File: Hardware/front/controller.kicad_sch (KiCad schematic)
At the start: 15 parts

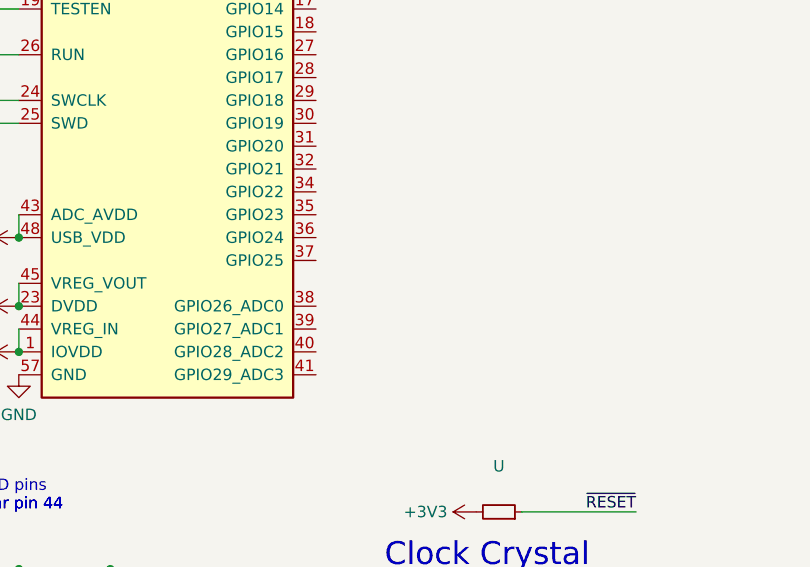
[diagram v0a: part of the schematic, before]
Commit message: hw: more front panel stuff
- fixed the mirrored pinout for the connector to the controller board

- Replaced a few capacitors to reduce BOM count

- Start connecting signals to RP2040, including the flash connection
  (dedicated to it)
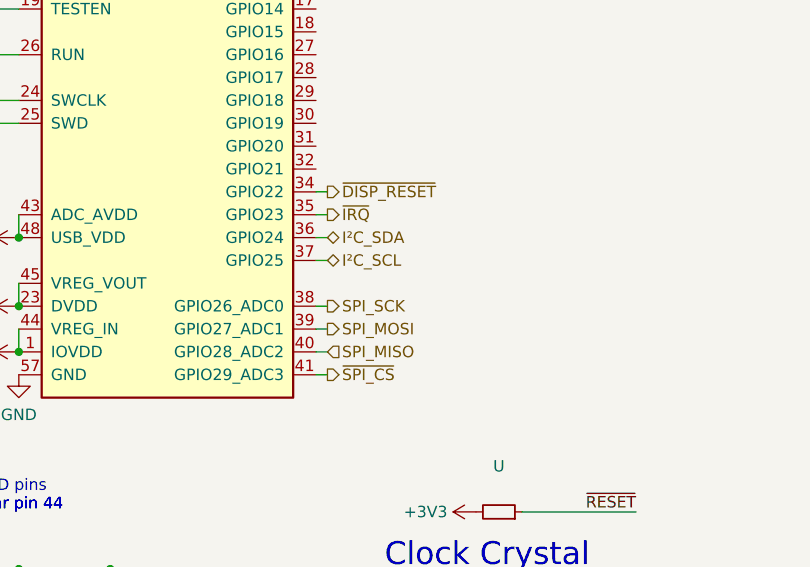
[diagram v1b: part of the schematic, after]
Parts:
- U: JLCPCB (none) -> C19666
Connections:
- net ~{DISP_RESET}: now reaches U.34 (GPIO22)
- net ~{IRQ}: now reaches U.35 (GPIO23)
- net I²C_SDA: now reaches U.36 (GPIO24)
- net I²C_SCL: now reaches U.37 (GPIO25)
- net SPI_SCK: now reaches U.38 (GPIO26_ADC0)
- net SPI_MOSI: now reaches U.39 (GPIO27_ADC1)
- net SPI_MISO: now reaches U.40 (GPIO28_ADC2)
- net ~{SPI_CS}: now reaches U.41 (GPIO29_ADC3)
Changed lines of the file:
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@@
+    (stroke (width 0) (type default))
+  )
+  (wire (pts (xy 68.58 93.98) (xy 69.85 93.98))
     (stroke (width 0) (type default))
   )
@@
     (stroke (width 0) (type default))
   )
+  (wire (pts (xy 68.58 91.44) (xy 69.85 91.44))
+    (stroke (width 0) (type default))
+  )
   (wire (pts (xy 35.56 147.32) (xy 45.72 147.32))
     (stroke (width 0) (type default))
@@
     (stroke (width 0) (type default))
   )
+  (wire (pts (xy 68.58 78.74) (xy 69.85 78.74))
+    (stroke (width 0) (type default))
+  )
   (wire (pts (xy 101.6 173.355) (xy 114.3 173.355))
     (stroke (width 0) (type default))
@@
     (stroke (width 0) (type default))
   )
+  (wire (pts (xy 68.58 99.06) (xy 69.85 99.06))
+    (stroke (width 0) (type default))
+  )
   (wire (pts (xy 45.72 125.73) (xy 55.88 125.73))
     (stroke (width 0) (type default))
@@
     (stroke (width 0) (type default))
   )
+  (wire (pts (xy 68.58 81.28) (xy 69.85 81.28))
+    (stroke (width 0) (type default))
+  )
   (wire (pts (xy 42.545 174.625) (xy 55.245 174.625))
     (stroke (width 0) (type default))
   )
+  (wire (pts (xy 68.58 96.52) (xy 69.85 96.52))
+    (stroke (width 0) (type default))
+  )
   (wire (pts (xy 35.56 36.83) (xy 22.86 36.83))
     (stroke (width 0) (type default))
@@
     (stroke (width 0) (type default))
   )
+  (wire (pts (xy 68.58 83.82) (xy 69.85 83.82))
+    (stroke (width 0) (type default))
+  )
   (wire (pts (xy 35.56 34.29) (xy 22.86 34.29))
     (stroke (width 0) (type default))
@@
   )
   (wire (pts (xy 25.4 147.32) (xy 35.56 147.32))
+    (stroke (width 0) (type default))
+  )
+  (wire (pts (xy 68.58 86.36) (xy 69.85 86.36))
     (stroke (width 0) (type default))
   )
@@
   (label "XIN" (at 80.01 133.35 0) (fields_autoplaced)
     (effects (font (size 1.27 1.27)) (justify left bottom))
+  )
+  (hierarchical_label "I²C_SCL" (shape bidirectional) (at 69.85 86.36 0) (fields_autoplaced)
+    (effects (font (size 1.27 1.27)) (justify left))
+  )
+  (hierarchical_label "SPI_MOSI" (shape output) (at 69.85 93.98 0) (fields_autoplaced)
+    (effects (font (size 1.27 1.27)) (justify left))
+  )
+  (hierarchical_label "I²C_SDA" (shape bidirectional) (at 69.85 83.82 0) (fields_autoplaced)
+    (effects (font (size 1.27 1.27)) (justify left))
+  )
+  (hierarchical_label "SPI_SCK" (shape output) (at 69.85 91.44 0) (fields_autoplaced)
+    (effects (font (size 1.27 1.27)) (justify left))
+  )
+  (hierarchical_label "~{SPI_CS}" (shape output) (at 69.85 99.06 0) (fields_autoplaced)
+    (effects (font (size 1.27 1.27)) (justify left))
+  )
+  (hierarchical_label "~{IRQ}" (shape output) (at 69.85 81.28 0) (fields_autoplaced)
+    (effects (font (size 1.27 1.27)) (justify left))
+  )
+  (hierarchical_label "~{DISP_RESET}" (shape output) (at 69.85 78.74 0) (fields_autoplaced)
+    (effects (font (size 1.27 1.27)) (justify left))
+  )
+  (hierarchical_label "SPI_MISO" (shape input) (at 69.85 96.52 0) (fields_autoplaced)
+    (effects (font (size 1.27 1.27)) (justify left))
   )
   (symbol (lib_id "Device:C_Small") (at 55.88 123.19 0) (mirror y) (unit 1)
@@
       (effects (font (size 1.27 1.27)) hide)
     )
+    (property "JLCPCB" "C19666" (id 5) (at 25.4 123.19 0)
+      (effects (font (size 1.27 1.27)) hide)
+    )
     (pin "1")
     (pin "2")
@@
       (effects (font (size 1.27 1.27)) hide)
     )
+    (property "JLCPCB" "C19666" (id 5) (at 25.4 144.78 0)
+      (effects (font (size 1.27 1.27)) hide)
+    )

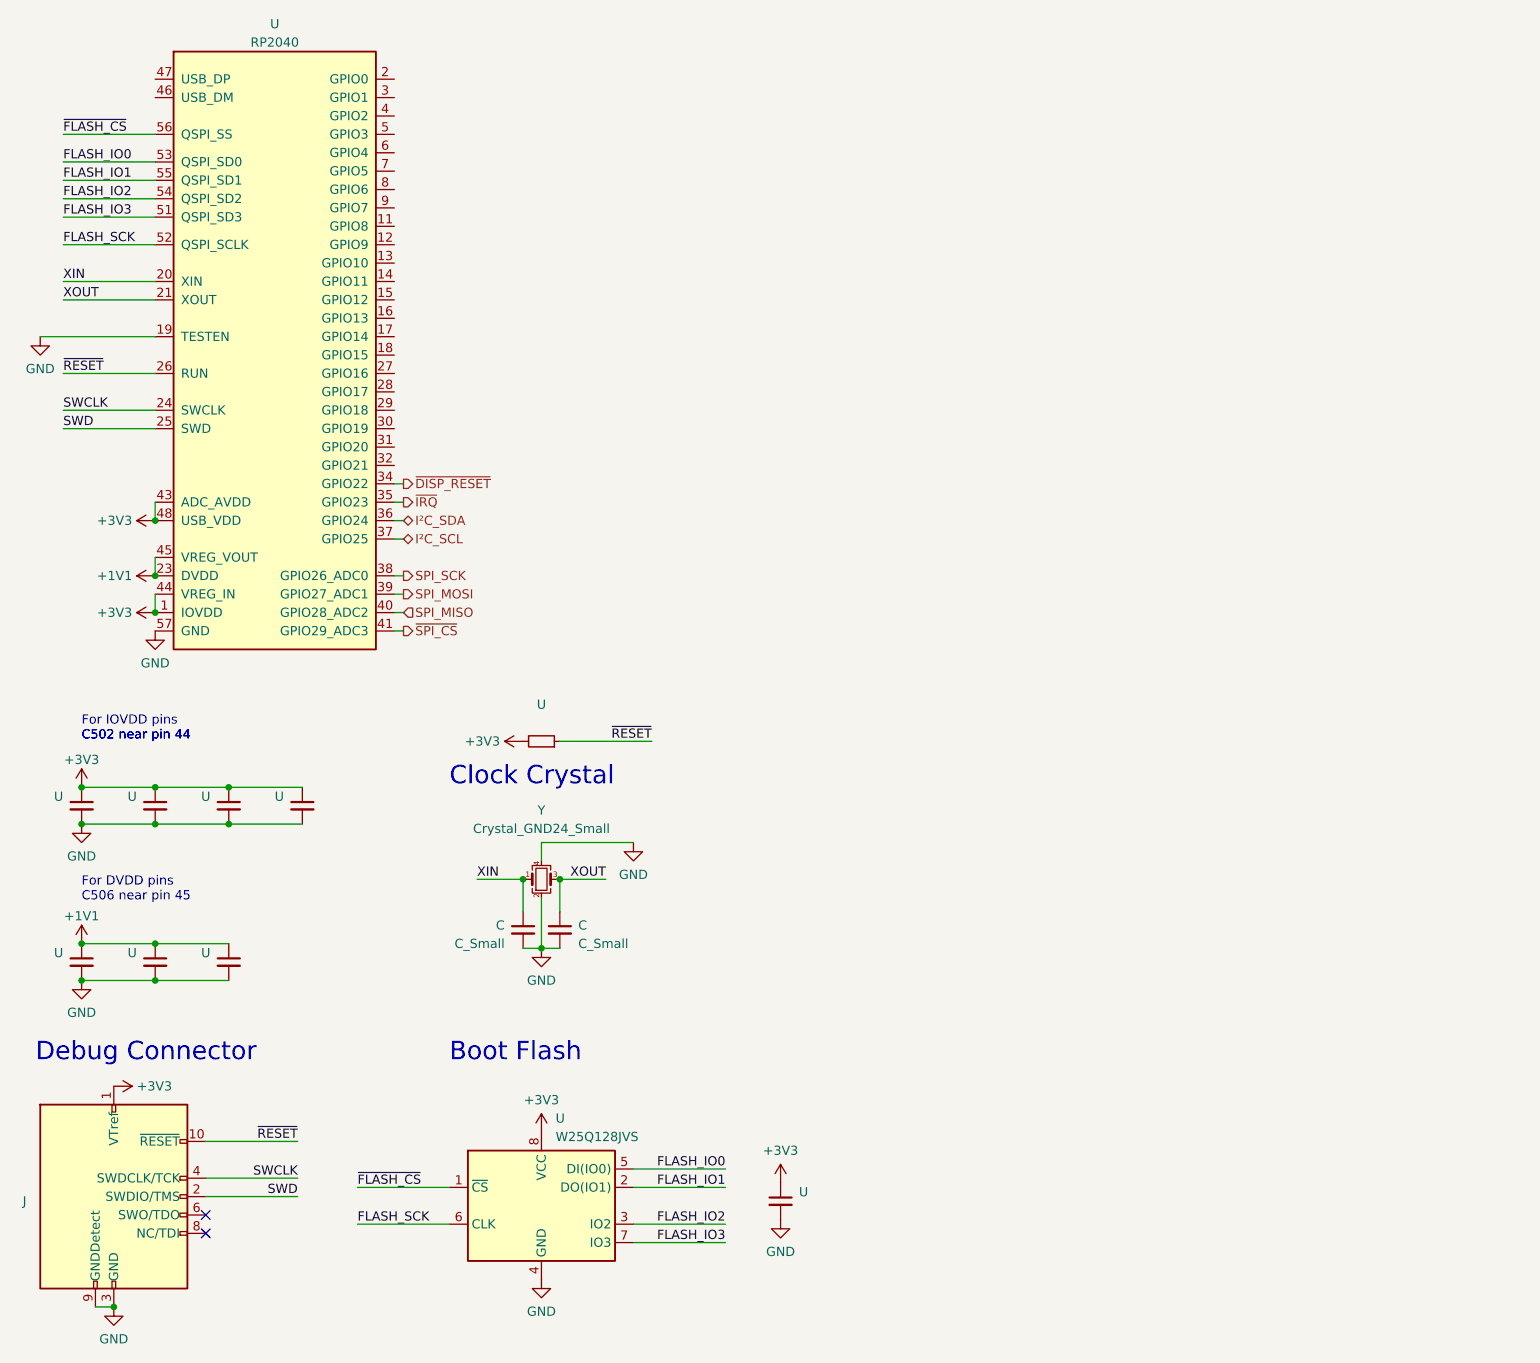
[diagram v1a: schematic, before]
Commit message: hw: First pass at new front panel
- Finished routing all signals on the front panel

- Put back the LED controller (PCA9955B) since that's a very nice and
  convenient way to drive the LEDs; it's driven via a "private" I2C bus
  from the RP2040 instead of the host controlling it.

  The touch panel controller is also hanging off this private bus so we
  can deal with it.

- Made trigger LED bicolor (green/orange)
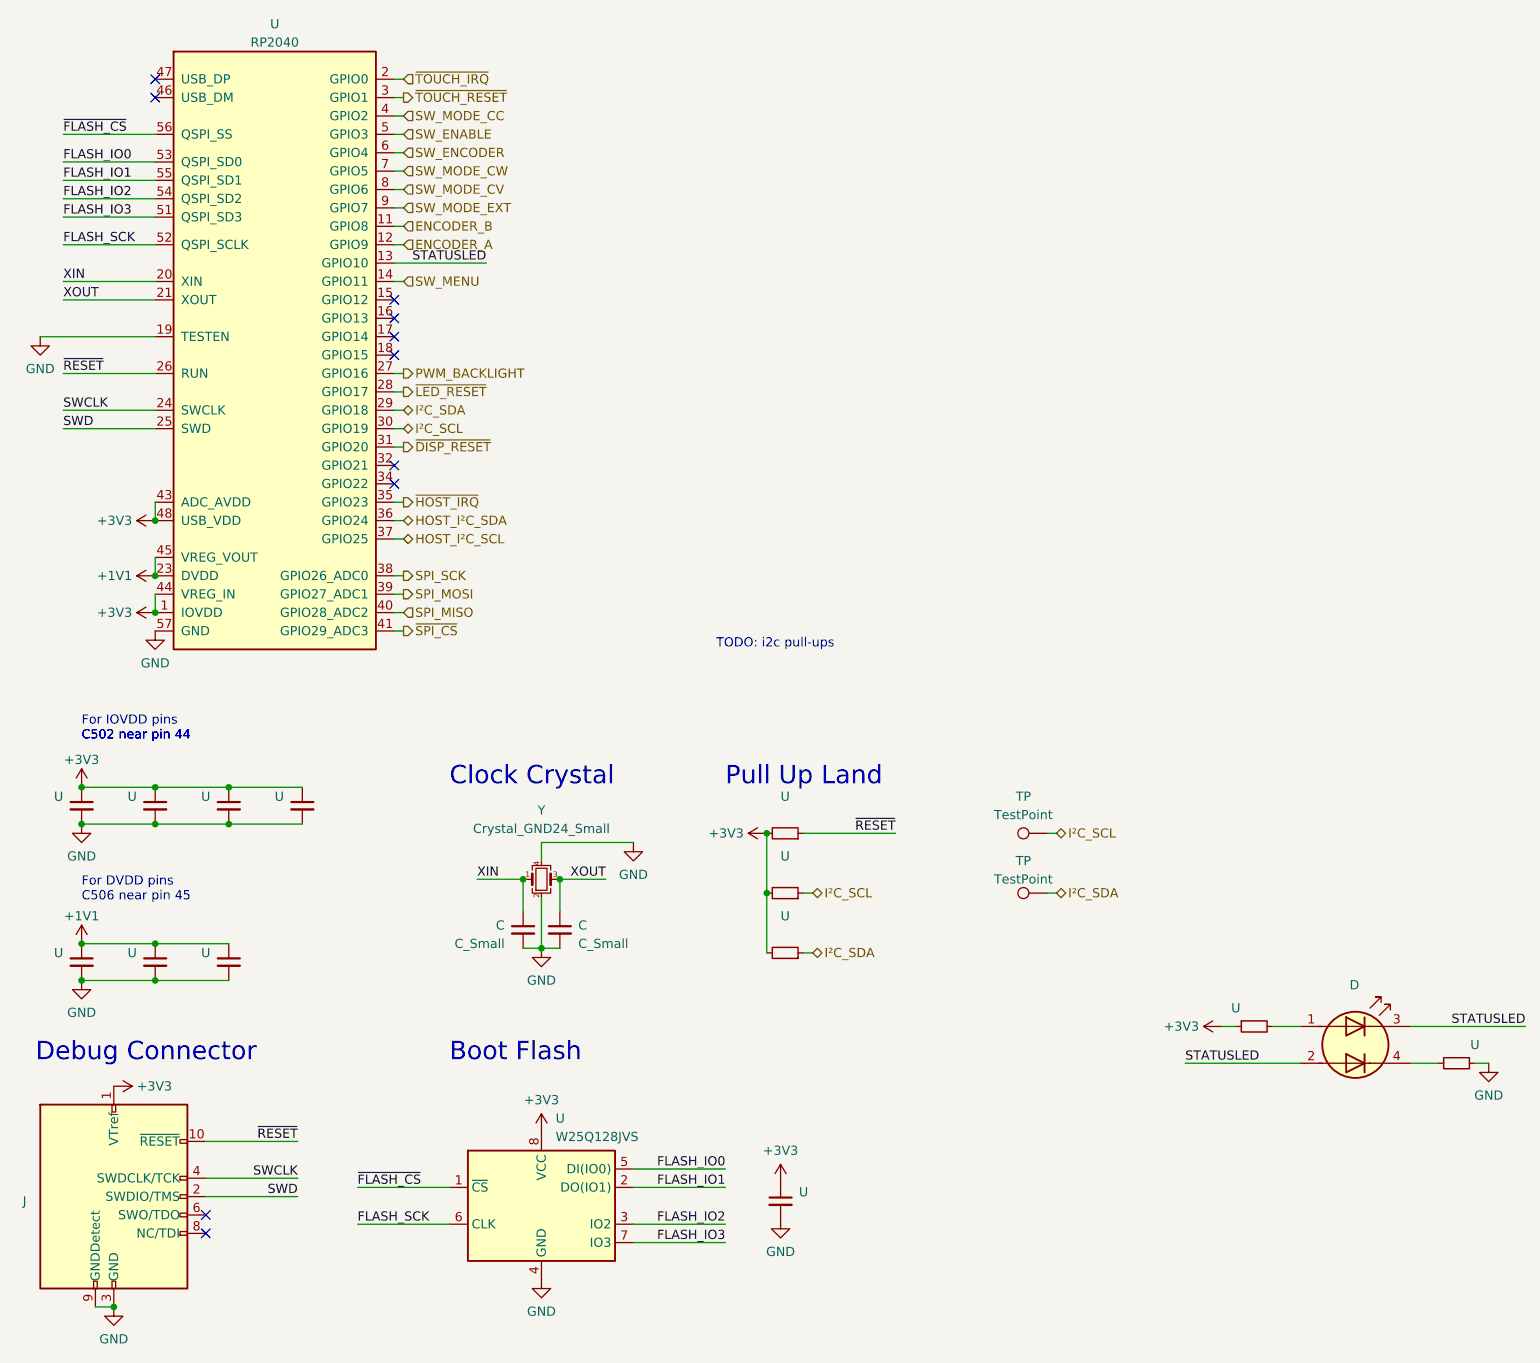
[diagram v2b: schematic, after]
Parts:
- added D: LED_Dual_AAKK, symbol Device:LED_Dual_AAKK
- added TP (x2): TestPoint, symbol Connector:TestPoint
- added U (x4): (no value), symbol Device:R_Small
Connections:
- net +3V3: now also U.1, U.2, U.2
- net GND: now also U.1
- net I²C_SCL: now also U.30 (GPIO19), TP.1, U.1; no longer U.37 (GPIO25)
- net I²C_SDA: now also U.29 (GPIO18), TP.1, U.1; no longer U.36 (GPIO24)
- net ~{DISP_RESET}: now also U.31 (GPIO20); no longer U.34 (GPIO22)
- net ENCODER_B: now reaches U.11 (GPIO8)
- net ENCODER_A: now reaches U.12 (GPIO9)
- net STATUSLED: now reaches U.13 (GPIO10)
- net STATUSLED: now also D.2 (A2), D.3 (K1)
- net SW_MENU: now reaches U.14 (GPIO11)
- net ~{TOUCH_IRQ}: now reaches U.2 (GPIO0)
- net PWM_BACKLIGHT: now reaches U.27 (GPIO16)
- net ~{LED_RESET}: now reaches U.28 (GPIO17)
- net ~{TOUCH_RESET}: now reaches U.3 (GPIO1)
- net SW_MODE_CC: now reaches U.4 (GPIO2)
- net SW_ENABLE: now reaches U.5 (GPIO3)
- net SW_ENCODER: now reaches U.6 (GPIO4)
- net SW_MODE_CW: now reaches U.7 (GPIO5)
- net SW_MODE_CV: now reaches U.8 (GPIO6)
- net SW_MODE_EXT: now reaches U.9 (GPIO7)
- net ~{IRQ} renamed ~{HOST_IRQ}
- new net: D.1 (A1), U.2
- new net: D.4 (K2), U.2
- new net HOST_I²C_SCL: U.37 (GPIO25)
- new net HOST_I²C_SDA: U.36 (GPIO24)
- no-connect marks 2 -> 10
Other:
- note added: "Pull Up Land"
- note added: "TODO: i2c pull-ups"
- moved on the sheet: U

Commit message: updated front panel pinout
- added system reset, direct load on/off switch output lines

- added separate touch screen reset/interrupt lines (the touch
  controller gets to be driven by linux side)

- update footprint for ER-TFT040-1 display

  this tweaks the sizes of the openings and the text labels a bit to be
  prettier
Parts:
- U: JLCPCB (none) -> C14663
- U: JLCPCB (none) -> C2040
- U: JLCPCB (none) -> C97521
- U: JLCPCB (none) -> C21190
- U: JLCPCB (none) -> C25804
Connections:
- net ~{TOUCH_IRQ}: no longer names the net of U.2 (GPIO0)
- net ~{TOUCH_RESET} renamed ~{SYS_RESET}
- no-connect marks 10 -> 11
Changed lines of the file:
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@@
   (no_connect (at 42.545 179.705))
   (no_connect (at 35.56 22.86))
+  (no_connect (at 68.58 22.86))
   (no_connect (at 68.58 55.88))
   (no_connect (at 42.545 182.245))
@@
     (stroke (width 0) (type default))
   )
-  (wire (pts (xy 68.58 22.86) (xy 69.85 22.86))
-    (stroke (width 0) (type default))
-  )
   (wire (pts (xy 68.58 45.72) (xy 69.85 45.72))
     (stroke (width 0) (type default))
@@
     (stroke (width 0) (type default))
   )
+  (wire (pts (xy 86.36 133.35) (xy 86.36 137.795))
+    (stroke (width 0) (type default))
+  )
+  (wire (pts (xy 22.86 71.12) (xy 35.56 71.12))
+    (stroke (width 0) (type default))
+  )
+  (wire (pts (xy 68.58 43.18) (xy 69.85 43.18))
+    (stroke (width 0) (type default))
+  )
+  (wire (pts (xy 22.86 45.72) (xy 35.56 45.72))
+    (stroke (width 0) (type default))
+  )
+  (wire (pts (xy 22.86 63.5) (xy 35.56 63.5))
+    (stroke (width 0) (type default))
+  )
+  (wire (pts (xy 68.58 99.06) (xy 69.85 99.06))
+    (stroke (width 0) (type default))
+  )
+  (wire (pts (xy 45.72 125.73) (xy 55.88 125.73))
+    (stroke (width 0) (type default))
+  )
+  (wire (pts (xy 35.56 88.9) (xy 35.56 91.44))
+    (stroke (width 0) (type default))
+  )
+  (wire (pts (xy 35.56 125.73) (xy 45.72 125.73))
+    (stroke (width 0) (type default))
+  )
+  (wire (pts (xy 42.545 169.545) (xy 55.245 169.545))
+    (stroke (width 0) (type default))
+  )
+  (wire (pts (xy 68.58 63.5) (xy 69.85 63.5))
+    (stroke (width 0) (type default))
+  )
+  (wire (pts (xy 35.56 39.37) (xy 22.86 39.37))
+    (stroke (width 0) (type default))
+  )
+  (wire (pts (xy 217.805 158.75) (xy 219.71 158.75))
+    (stroke (width 0) (type default))
+  )
   (wire (pts (xy 68.58 25.4) (xy 69.85 25.4))
-    (stroke (width 0) (type default))
-  )
-  (wire (pts (xy 86.36 133.35) (xy 86.36 137.795))
-    (stroke (width 0) (type default))
-  )
-  (wire (pts (xy 22.86 71.12) (xy 35.56 71.12))
-    (stroke (width 0) (type default))
-  )
-  (wire (pts (xy 68.58 43.18) (xy 69.85 43.18))
-    (stroke (width 0) (type default))
-  )
-  (wire (pts (xy 22.86 45.72) (xy 35.56 45.72))
-    (stroke (width 0) (type default))
-  )
-  (wire (pts (xy 22.86 63.5) (xy 35.56 63.5))
-    (stroke (width 0) (type default))
-  )
-  (wire (pts (xy 68.58 99.06) (xy 69.85 99.06))
-    (stroke (width 0) (type default))
-  )
-  (wire (pts (xy 45.72 125.73) (xy 55.88 125.73))
-    (stroke (width 0) (type default))
-  )
-  (wire (pts (xy 35.56 88.9) (xy 35.56 91.44))
-    (stroke (width 0) (type default))
-  )
-  (wire (pts (xy 35.56 125.73) (xy 45.72 125.73))
-    (stroke (width 0) (type default))
-  )
-  (wire (pts (xy 42.545 169.545) (xy 55.245 169.545))
-    (stroke (width 0) (type default))
-  )
-  (wire (pts (xy 68.58 63.5) (xy 69.85 63.5))
-    (stroke (width 0) (type default))
-  )
-  (wire (pts (xy 35.56 39.37) (xy 22.86 39.37))
-    (stroke (width 0) (type default))
-  )
-  (wire (pts (xy 217.805 158.75) (xy 219.71 158.75))
     (stroke (width 0) (type default))
   )
@@
     (effects (font (size 1.27 1.27)) (justify left))
   )
-  (hierarchical_label "~{TOUCH_IRQ}" (shape input) (at 69.85 22.86 0) (fields_autoplaced)
+  (hierarchical_label "~{SYS_RESET}" (shape output) (at 69.85 25.4 0) (fields_autoplaced)
     (effects (font (size 1.27 1.27)) (justify left))
   )
@@
   )
   (hierarchical_label "SPI_MISO" (shape input) (at 69.85 96.52 0) (fields_autoplaced)
-    (effects (font (size 1.27 1.27)) (justify left))
-  )
-  (hierarchical_label "~{TOUCH_RESET}" (shape output) (at 69.85 25.4 0) (fields_autoplaced)
     (effects (font (size 1.27 1.27)) (justify left))
   )
@@
     )
     (property "MPN" "" (id 4) (at 55.88 123.19 0)
+      (effects (font (size 1.27 1.27)) hide)
+    )
+    (property "JLCPCB" "C14663" (id 5) (at 55.88 123.19 0)
       (effects (font (size 1.27 1.27)) hide)
     )
@@
     )
     (property "Datasheet" "https://datasheets.raspberrypi.com/rp2040/rp2040-datasheet.pdf" (id 3) (at 58.42 3.81 0)
+      (effects (font (size 1.27 1.27)) hide)
+    )
+    (property "JLCPCB" "C2040" (id 4) (at 52.07 19.05 0)
       (effects (font (size 1.27 1.27)) hide)
     )
@@
       (effects (font (size 1.27 1.27)) hide)
     )
+    (property "JLCPCB" "C14663" (id 5) (at 45.72 144.78 0)
+      (effects (font (size 1.27 1.27)) hide)
+    )
     (pin "1")
     (pin "2")
@@
     )
     (property "Datasheet" "http://www.winbond.com/resource-files/w25q128jv_dtr%20revc%2003272018%20plus.pdf" (id 3) (at 88.9 178.435 0)
+      (effects (font (size 1.27 1.27)) hide)
+    )
+    (property "JLCPCB" "C97521" (id 4) (at 88.9 178.435 0)
       (effects (font (size 1.27 1.27)) hide)
     )
@@
     )
     (property "MPN" "" (id 4) (at 45.72 123.19 0)
+      (effects (font (size 1.27 1.27)) hide)
+    )
+    (property "JLCPCB" "C14663" (id 5) (at 45.72 123.19 0)
       (effects (font (size 1.27 1.27)) hide)
     )
@@
       (effects (font (size 1.27 1.27)) hide)
     )
+    (property "JLCPCB" "C14663" (id 5) (at 121.92 177.8 0)
+      (effects (font (size 1.27 1.27)) hide)
+    )
     (pin "1")
     (pin "2")
@@
       (effects (font (size 1.27 1.27)) hide)
     )
+    (property "JLCPCB" "C21190" (id 5) (at 187.325 153.67 90)
+      (effects (font (size 1.27 1.27)) hide)
+    )
     (pin "1")
     (pin "2")
@@
     )
     (property "MPN" "" (id 4) (at 122.555 127 90)
+      (effects (font (size 1.27 1.27)) hide)
+    )
+    (property "JLCPCB" "C25804" (id 5) (at 122.555 127 90)
       (effects (font (size 1.27 1.27)) hide)
     )
@@
       (effects (font (size 1.27 1.27)) hide)
     )
+    (property "JLCPCB" "C14663" (id 5) (at 35.56 144.78 0)
+      (effects (font (size 1.27 1.27)) hide)
+    )
     (pin "1")
     (pin "2")
@@
       (effects (font (size 1.27 1.27)) hide)
     )
+    (property "JLCPCB" "C21190" (id 5) (at 215.265 158.75 90)
+      (effects (font (size 1.27 1.27)) hide)
+    )
     (pin "1")
     (pin "2")
@@
       (effects (font (size 1.27 1.27)) hide)
     )
+    (property "JLCPCB" "C14663" (id 5) (at 35.56 123.19 0)
+      (effects (font (size 1.27 1.27)) hide)
+    )
